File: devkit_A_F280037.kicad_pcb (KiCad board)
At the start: 2 copper layers, 90 x 45 mm, 0 parts

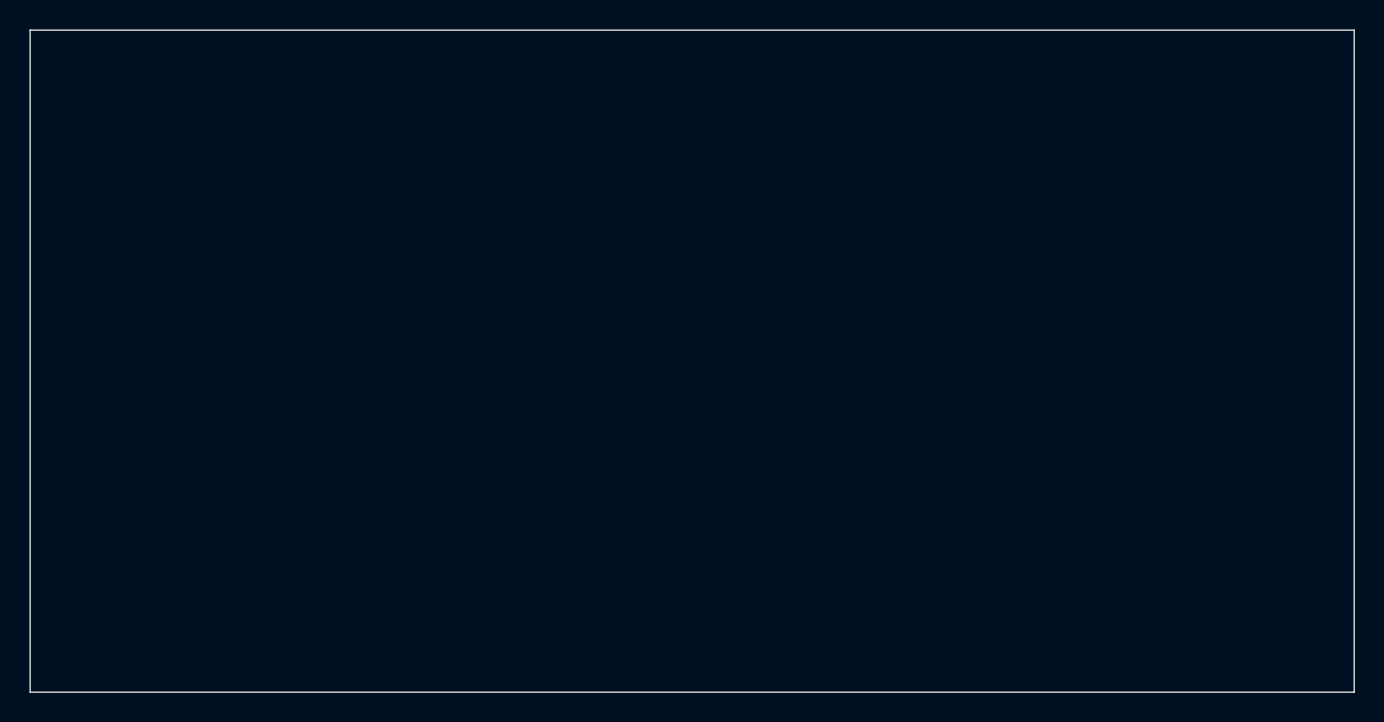
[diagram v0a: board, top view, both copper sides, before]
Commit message: spec-devkit.md devient la source de verite unique, brochage-devkit.md fusionne
La specification consolidee fournie remplace, comme elle l'annonce elle-meme,
tous les documents de brochage anterieurs. Verifiee contre
lib/C2000_Devkit_Connectors.kicad_sym: 56 positions sur 56, zero ecart.

brochage-devkit.md dupliquait desormais les memes 56 positions dans une autre
mise en forme — le mode de defaillance exact qui vient de couter trois semaines
de divergence. Il est reduit a ce qu'il avait d'unique et renomme
nappes-shield.md: les quatre nappes vers la carte de puissance, et la
repartition des cartes.

La specification apporte trois choses absentes du depot: l'entraxe 25,4 mm des
rangees (contre 22,86 mm pour l'ESP32, soit deux references de support sur le
shield), la valeur OTP BOOTPIN_CONFIG = 0x5AFF18FF, et l'obligation d'ecrire
GPIOHAMSEL pour piloter GPIO20/GPIO21 en numerique sur le F28P551.

Le contour du devkit passe de 90 x 45 a 75 x 28 mm: il portait « dimension a
confirmer », elle l'est.

Conflit non tranche, porte dans les points ouverts: la specification recommande
quatre couches pour un plan de masse continu sous la zone analogique, la
contrainte de fabrication du CLAUDE.md en pose deux.

Co-Authored-By: Claude Opus 5 <noreply@anthropic.com>
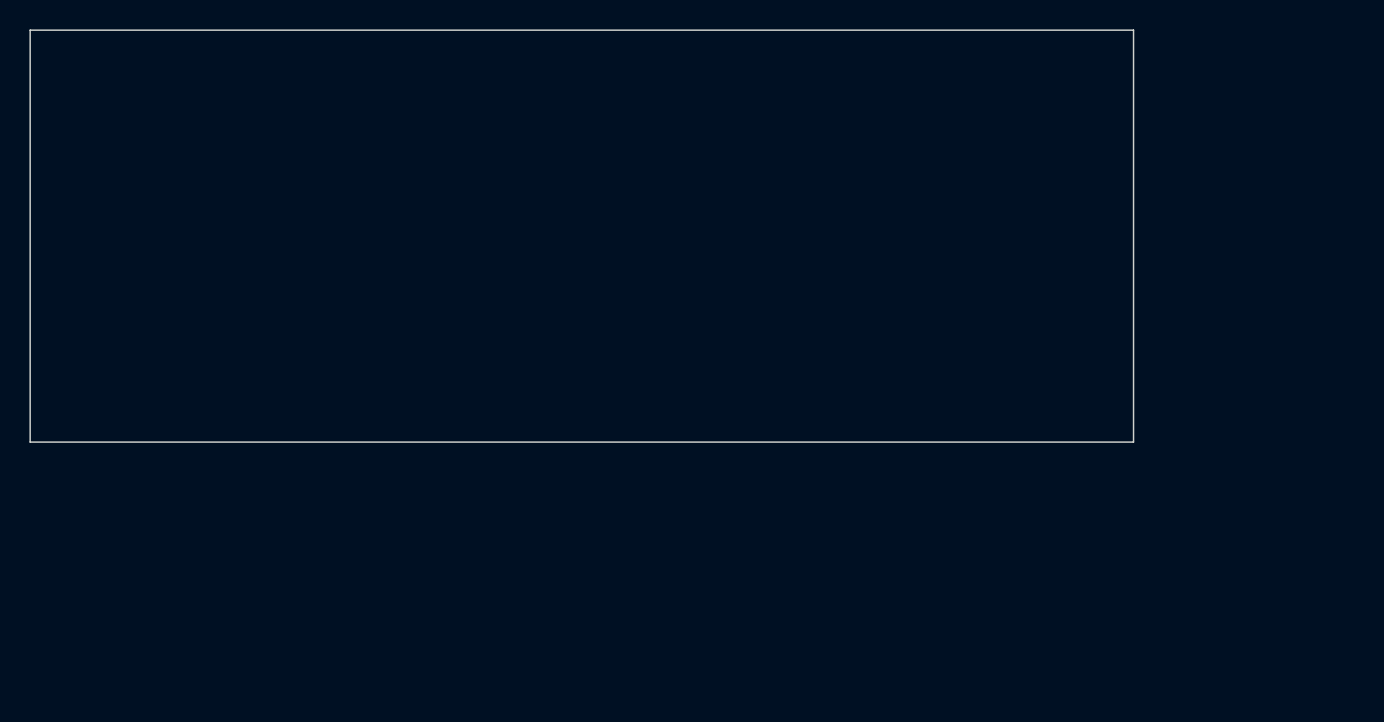
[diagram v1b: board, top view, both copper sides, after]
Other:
- board size 90 x 45 mm -> 75 x 28 mm
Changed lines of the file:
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@@
 	)
 	(net 0 "")
-	(gr_line (start 100.000 80.000) (end 190.000 80.000)
+	(gr_line (start 100.000 80.000) (end 175.000 80.000)
 		(stroke (width 0.1) (type default)) (layer "Edge.Cuts")
 	)
-	(gr_line (start 190.000 80.000) (end 190.000 125.000)
+	(gr_line (start 175.000 80.000) (end 175.000 108.000)
 		(stroke (width 0.1) (type default)) (layer "Edge.Cuts")
 	)
-	(gr_line (start 190.000 125.000) (end 100.000 125.000)
+	(gr_line (start 175.000 108.000) (end 100.000 108.000)
 		(stroke (width 0.1) (type default)) (layer "Edge.Cuts")
 	)
-	(gr_line (start 100.000 125.000) (end 100.000 80.000)
+	(gr_line (start 100.000 108.000) (end 100.000 80.000)
 		(stroke (width 0.1) (type default)) (layer "Edge.Cuts")
 	)

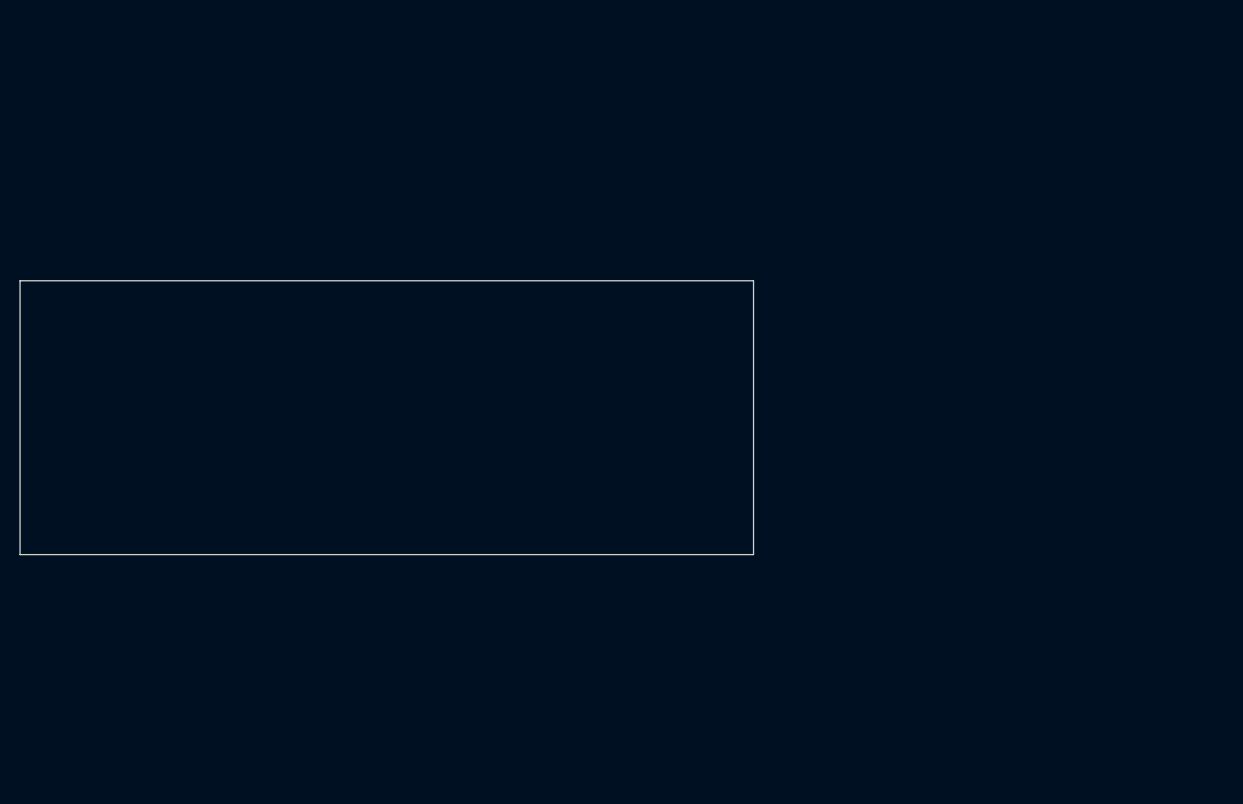
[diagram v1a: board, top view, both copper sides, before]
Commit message: PCB du devkit A peuple: 27 empreintes, les deux cartes convergent
Le F8 passe sans erreur sur le A, avec le TC2050 a la place de l'ancienne
embase. Les deux PCB portent desormais les memes 27 empreintes.

DRC identique de part et d'autre a une violation de serigraphie pres: 106
elements non connectes, 61 annular_width, ~60 clearance. Aucun n'a de sens a
ce stade — les empreintes arrivent empilees et rien n'est place ni route. Les
annular_width viennent de la confrontation entre les empreintes standard et
les regles de gravure maison (via 2 mm, percage 0,8 mm); c'est exactement la
tension que la decision 12 anticipe entre les deux variantes de fabrication.

Co-Authored-By: Claude Opus 5 <noreply@anthropic.com>
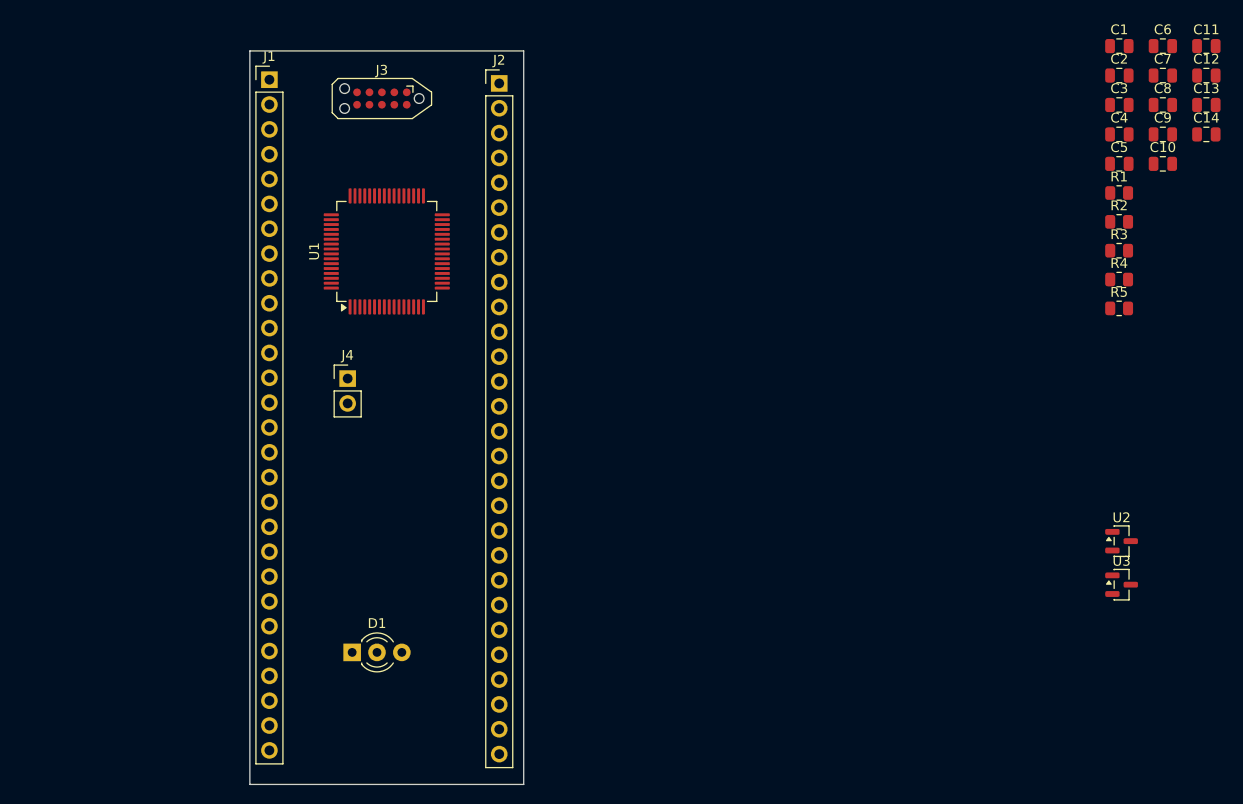
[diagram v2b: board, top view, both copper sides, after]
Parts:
- added C1: 10u, Capacitor_SMD:C_0805_2012Metric, F.Cu at (212.4, 56.0)
- added C10: 100n, Capacitor_SMD:C_0805_2012Metric, F.Cu at (216.9, 68.0)
- added C11: 100n, Capacitor_SMD:C_0805_2012Metric, F.Cu at (221.3, 56.0)
- added C12: 10u, Capacitor_SMD:C_0805_2012Metric, F.Cu at (221.3, 59.0)
- added C13: 2u2, Capacitor_SMD:C_0805_2012Metric, F.Cu at (221.3, 62.0)
- added C14: 100n, Capacitor_SMD:C_0805_2012Metric, F.Cu at (221.3, 65.0)
- added C2: 10u, Capacitor_SMD:C_0805_2012Metric, F.Cu at (212.4, 59.0)
- added C3: 10u, Capacitor_SMD:C_0805_2012Metric, F.Cu at (212.4, 62.0)
- added C4: 10u, Capacitor_SMD:C_0805_2012Metric, F.Cu at (212.4, 65.0)
- added C5: 100n, Capacitor_SMD:C_0805_2012Metric, F.Cu at (212.4, 68.0)
- added C6: 100n, Capacitor_SMD:C_0805_2012Metric, F.Cu at (216.9, 56.0)
- added C7: 2u2, Capacitor_SMD:C_0805_2012Metric, F.Cu at (216.9, 59.0)
- added C8: 100n, Capacitor_SMD:C_0805_2012Metric, F.Cu at (216.9, 62.0)
- added C9: 100n, Capacitor_SMD:C_0805_2012Metric, F.Cu at (216.9, 65.0)
- added D1: LED_BICOLORE_3MM, LED_THT:LED_D3.0mm-3, F.Cu at (134.0, 118.0)
- added J1: DEVKIT_C2000_ROW_A, Connector_PinHeader_2.54mm:PinHeader_1x28_P2.54mm_Vertical, F.Cu at (125.5, 59.4)
- added J2: DEVKIT_C2000_ROW_B, Connector_PinHeader_2.54mm:PinHeader_1x28_P2.54mm_Vertical, F.Cu at (149.0, 59.8)
- added J3: TC2050, Connector:Tag-Connect_TC2050-IDC-NL_2x05_P1.27mm_Vertical, F.Cu at (137.0, 61.4)
- added J4: RESET, Connector_PinHeader_2.54mm:PinHeader_1x02_P2.54mm_Vertical, F.Cu at (133.5, 90.0)
- added R1: 2k2, Resistor_SMD:R_0805_2012Metric, F.Cu at (212.4, 71.0)
- added R2: 10k, Resistor_SMD:R_0805_2012Metric, F.Cu at (212.4, 74.0)
- added R3: 10k, Resistor_SMD:R_0805_2012Metric, F.Cu at (212.4, 76.9)
- added R4: 10k, Resistor_SMD:R_0805_2012Metric, F.Cu at (212.4, 79.9)
- added R5: 1k, Resistor_SMD:R_0805_2012Metric, F.Cu at (212.4, 82.8)
- added U1: TMS320F280037CSPM, Package_QFP:LQFP-64_10x10mm_P0.5mm, F.Cu at (137.5, 77.0)
- added U2: MCP1700-3302E/TT, Package_TO_SOT_SMD:SOT-23, F.Cu at (212.6, 106.6)
- added U3: MCP1700-3302E/TT, Package_TO_SOT_SMD:SOT-23, F.Cu at (212.6, 111.1)
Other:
- board size 75 x 28 mm -> 28 x 75 mm
